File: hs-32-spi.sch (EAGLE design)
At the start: 18 parts, among them U1 RHD2132_QFN, U2 ADXL335

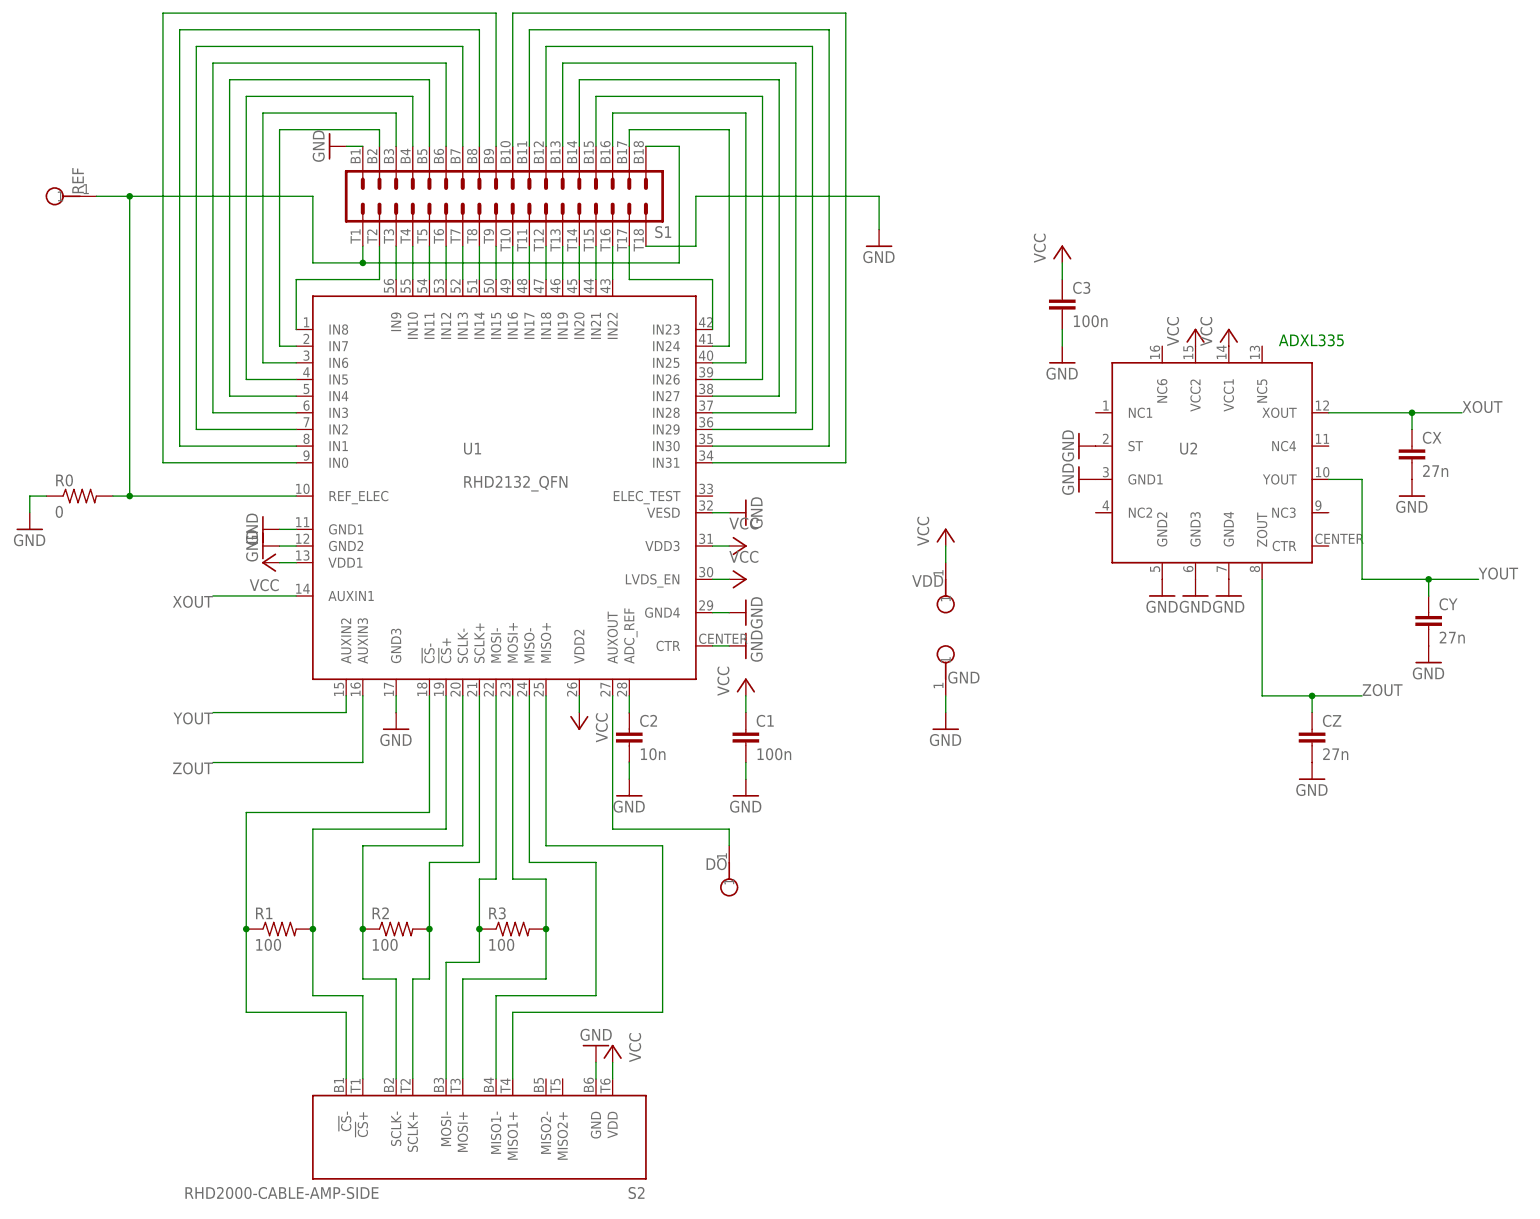
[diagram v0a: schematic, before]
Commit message: Added initial attempt of adding an expansion connector.
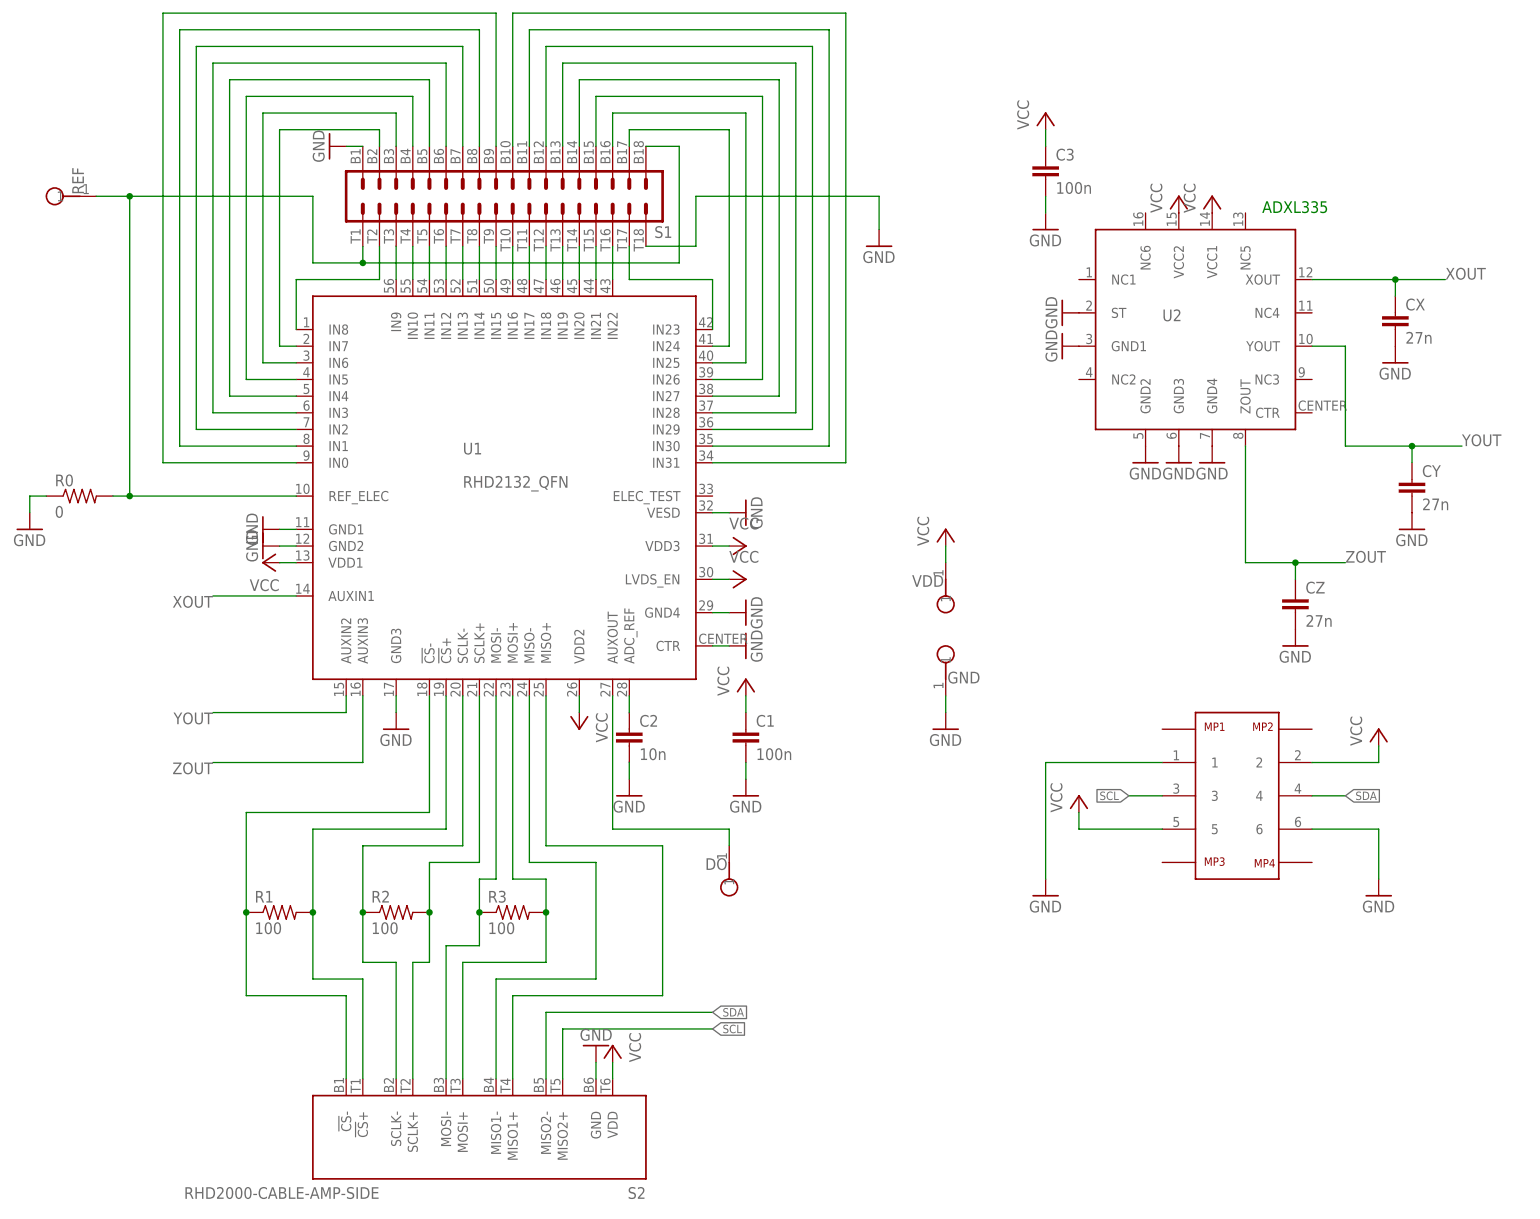
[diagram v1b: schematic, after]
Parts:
- added U3: (no value), Molex 5050700622:MOLEX_5050700622
- R1, R2, R3: device RHD2000_eval_board:R_0402 -> RHD2000_eval_board:R_0201
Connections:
- new net SCL: S2.MISO2+, U3.3
- new net SDA: S2.MISO2-, U3.4
- net GND: now also U3.1, U3.6
- net VCC: now also U3.2, U3.5
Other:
- moved on the sheet: C3, CX, CY, CZ, R1, R2, R3, U2
